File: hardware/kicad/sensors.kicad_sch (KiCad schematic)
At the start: 0 parts

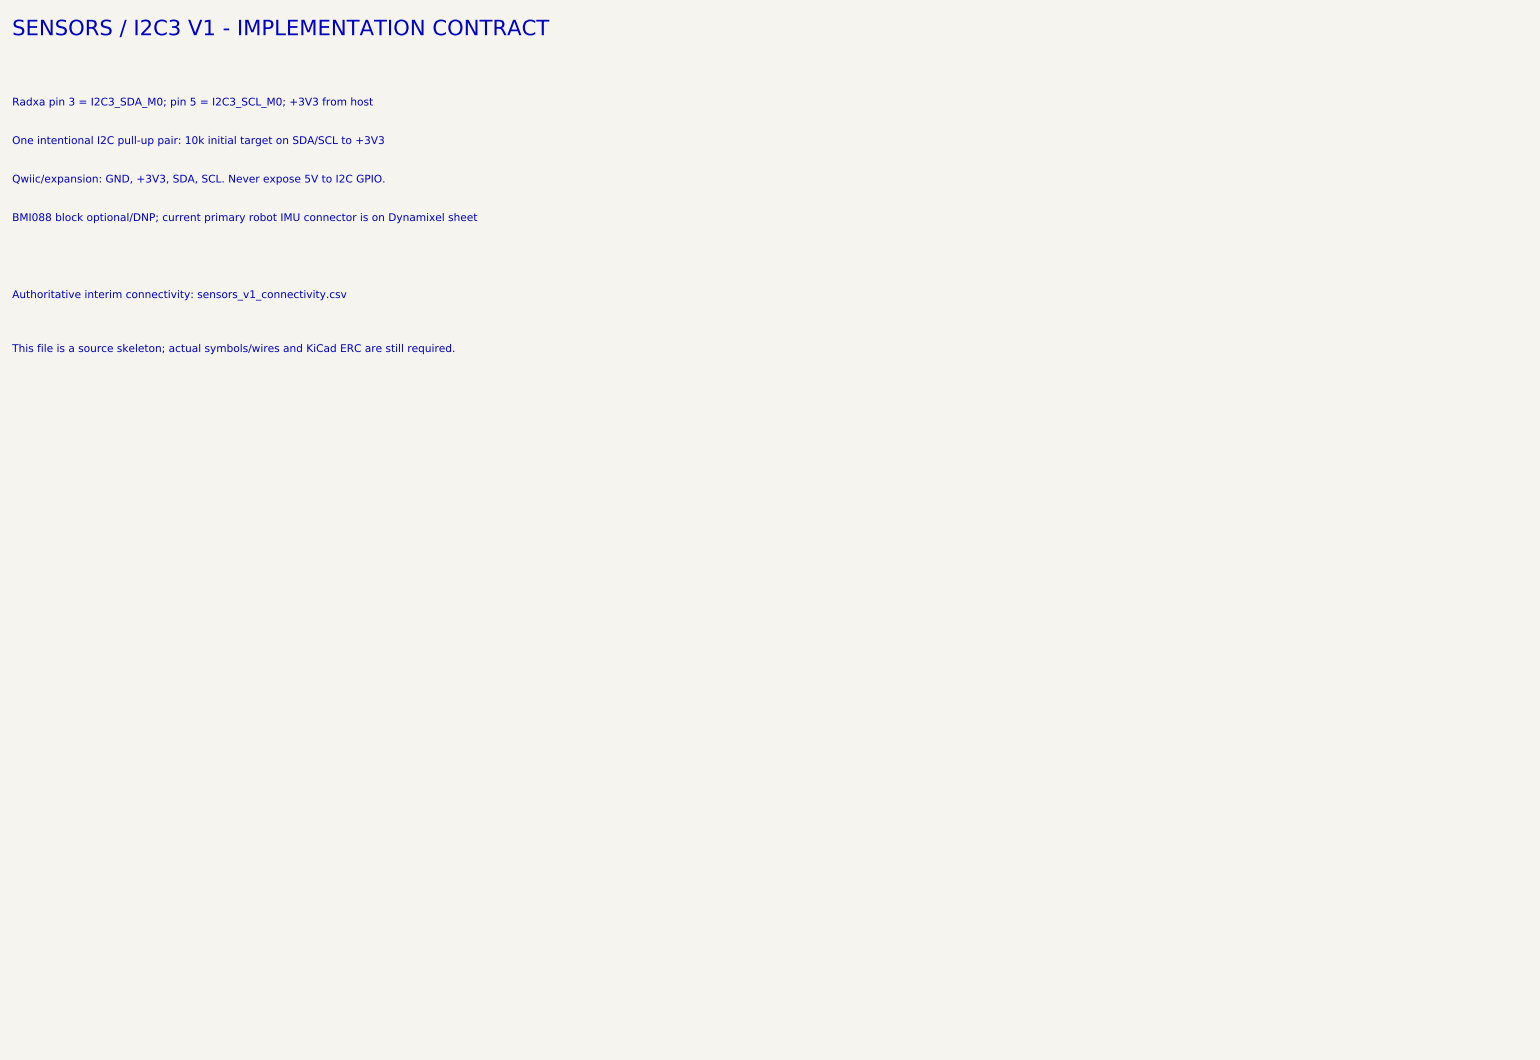
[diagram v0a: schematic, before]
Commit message: [verified] refactor(hardware): restore strict single-board Radxa port
Import the routed upstream Pollen Robot HAT as the active design, adapt the critical host nets for Radxa ZERO 3W, remove the divergent high-current redesign artifacts, and add regenerated baseline-aware KiCad validation.
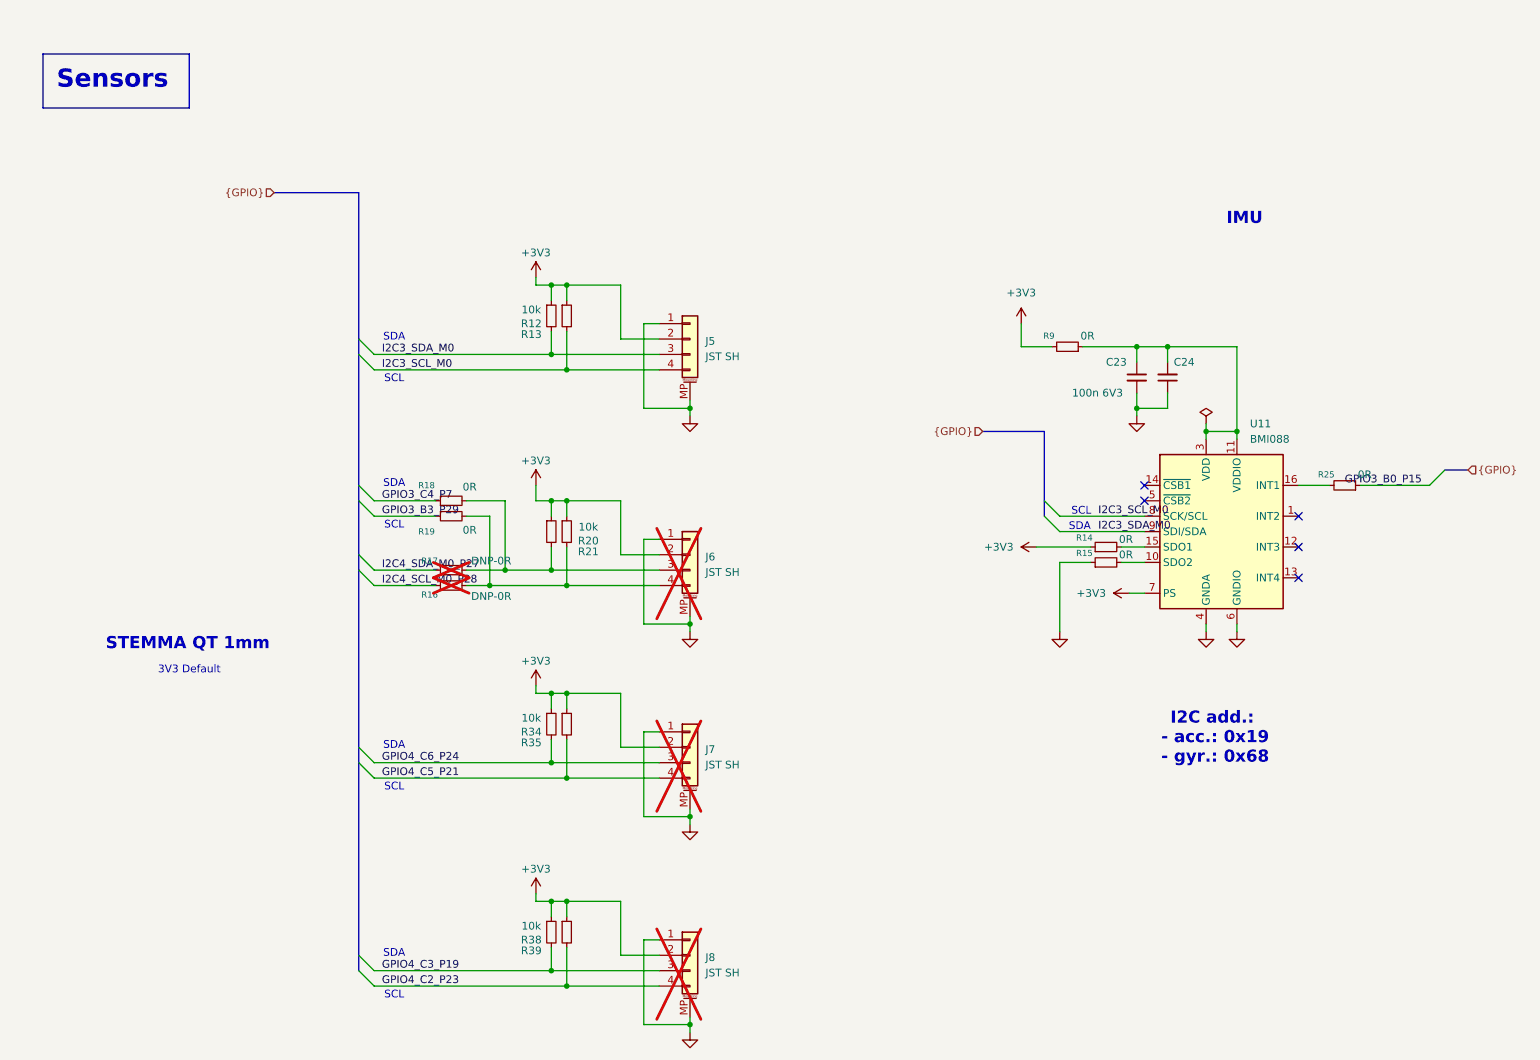
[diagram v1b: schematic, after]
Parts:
- added C23, C24: 100n 6V3, Capacitor_SMD:C_0402_1005Metric, symbol Device:C_Small
- added J5, J6, J7, J8: JST SH, Connector_JST:JST_SH_BM04B-SRSS-TB_1x04-1MP_P1.00mm_Vertical, symbol Connector_Generic_MountingPin:Conn_01x04_MountingPin
- added R12, R13, R20, R21, R34, R35, R38, R39: 10k, Resistor_SMD:R_0402_1005Metric, symbol Device:R_Small
- added R14, R15, R18, R19, R25, R9: 0R, Resistor_SMD:R_0402_1005Metric, symbol Device:R_Small
- added R16, R17: DNP-0R, Resistor_SMD:R_0402_1005Metric, symbol Device:R_Small
- added U11: BMI088, Package_LGA:Bosch_LGA-16_4.5x3mm_P0.5mm_LayoutBorder7x1y_ClockwisePinNumbering, symbol Sensor_Motion:BMI088
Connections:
- new net: J6.4 (Pin_4), R16.2, R19.2, R21.2
- new net: J6.3 (Pin_3), R17.2, R18.2, R20.2
- new net: R25.2, U11.16 (INT1)
- new net: R15.2, U11.10 (SDO2)
- new net: C23.1, C24.2, R9.1, U11.11 (VDDIO), U11.3 (VDD)
- new net: R14.2, U11.15 (SDO1)
- new net +3V3: J5.2 (Pin_2), J6.2 (Pin_2), J7.2 (Pin_2), J8.2 (Pin_2), R12.1, R13.1, R14.1, R20.1, R21.1, R34.1, R35.1, R38.1, R39.1, R9.2, U11.7 (PS)
- new net GND: C23.2, C24.1, J5.1 (Pin_1), J5.MP (MountPin), J6.1 (Pin_1), J6.MP (MountPin), J7.1 (Pin_1), J7.MP (MountPin), J8.1 (Pin_1), J8.MP (MountPin), R15.1, U11.2 (GNDA), U11.4 (GNDA), U11.6 (GNDIO)
- new net GPIO3_B0_P15: R25.1
- new net GPIO3_B3_P29: R19.1
- new net GPIO3_C4_P7: R18.1
- new net GPIO4_C2_P23: J8.4 (Pin_4), R39.2
- new net GPIO4_C3_P19: J8.3 (Pin_3), R38.2
- new net GPIO4_C5_P21: J7.4 (Pin_4), R35.2
- new net GPIO4_C6_P24: J7.3 (Pin_3), R34.2
- new net I2C3_SCL_M0: J5.4 (Pin_4), R13.2, U11.8 (SCK/SCL)
- new net I2C3_SDA_M0: J5.3 (Pin_3), R12.2, U11.9 (SDI/SDA)
- new net I2C4_SCL_M0_P28: R16.1
- new net I2C4_SDA_M0_P27: R17.1
- no-connect marks 0 -> 5
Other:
- note added: "3V3 Default"
- note added: "I2C add.: - acc.: 0x19 - gyr.: 0x68"
- note added: "IMU"
- note added: "SCL"
- note added: "SDA"
- note added: "STEMMA QT 1mm"
- note removed: "Authoritative interim connectivity: sensors_v1_connectivity.csv"
- note removed: "BMI088 block optional/DNP; current primary robot IMU connector is on Dynamixel sheet"
- note removed: "One intentional I2C pull-up pair: 10k initial target on SDA/SCL to +3V3"
- note removed: "Qwiic/expansion: GND, +3V3, SDA, SCL. Never expose 5V to I2C GPIO."
- note removed: "Radxa pin 3 = I2C3_SDA_M0; pin 5 = I2C3_SCL_M0; +3V3 from host"
- note removed: "SENSORS / I2C3 V1 - IMPLEMENTATION CONTRACT"
- note removed: "This file is a source skeleton; actual symbols/wires and KiCad ERC are still required."
- company: juper007 / DIY -> Pollen Robotics / Hugging Face
- title: Radxa ZERO 3W Robot HAT - Sensors / I2C V1 -> Radxa ZERO 3W Robot HAT

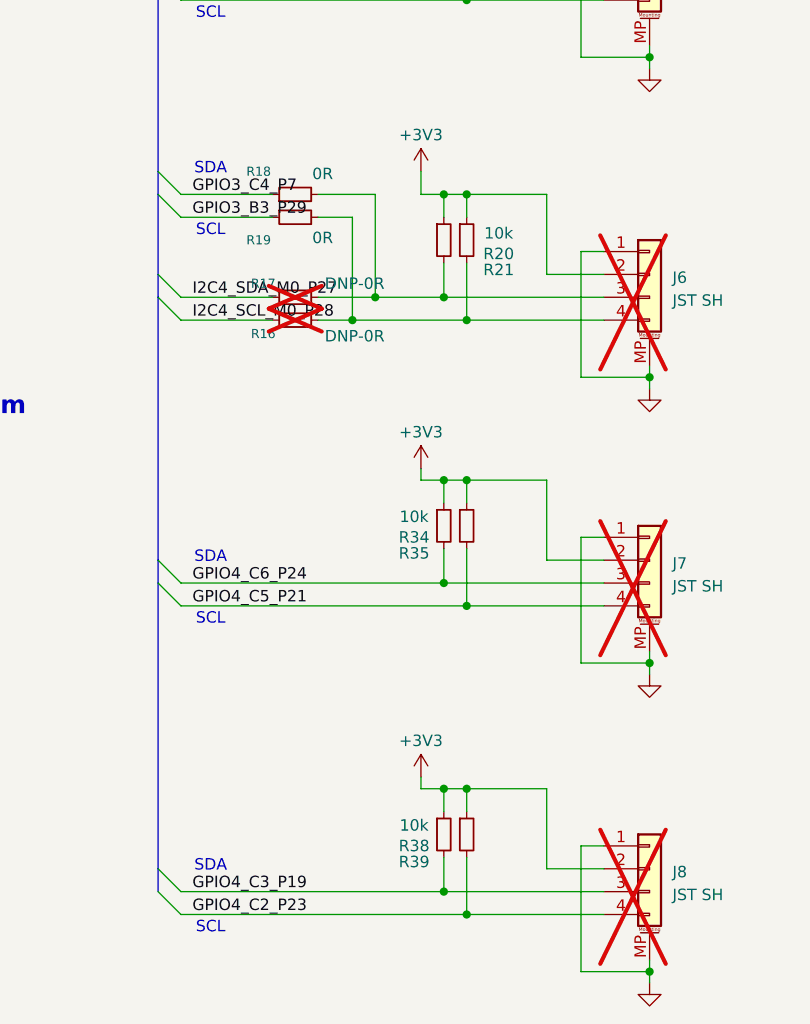
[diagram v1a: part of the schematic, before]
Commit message: [verified] fix(validation): enforce fail-closed strict-port guards
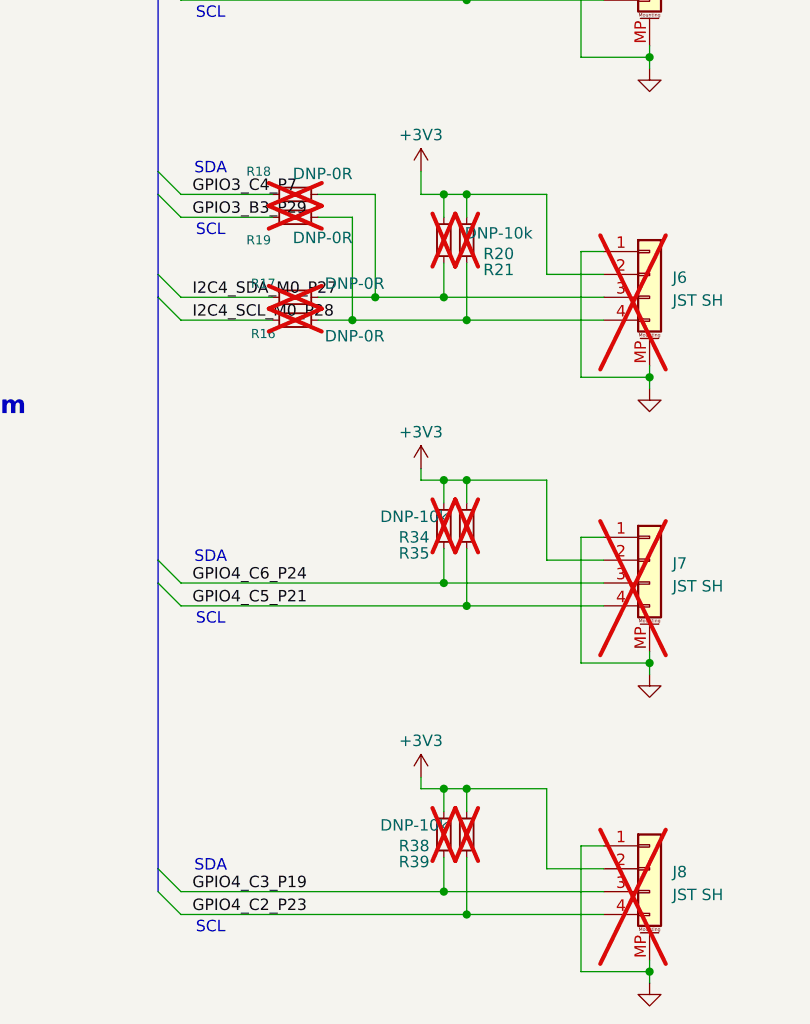
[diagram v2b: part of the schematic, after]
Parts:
- R18, R19: value 0R -> DNP-0R; now not fitted
- R20, R21, R34, R35, R38, R39: value 10k -> DNP-10k; now not fitted
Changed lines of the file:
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@@
 		(in_bom yes)
 		(on_board yes)
-		(dnp no)
+		(dnp yes)
 		(property "Reference" "R19"
 			(at 88.646 101.6 90)
@@
 			)
 		)
-		(property "Value" "0R"
+		(property "Value" "DNP-0R"
 			(at 95.758 101.346 90)
 			(effects
@@
 		(in_bom yes)
 		(on_board yes)
-		(dnp no)
+		(dnp yes)
 		(property "Reference" "R34"
 			(at 105.918 134.62 0)
@@
 			)
 		)
-		(property "Value" "10k"
+		(property "Value" "DNP-10k"
 			(at 105.918 132.334 0)
 			(effects
@@
 		(in_bom yes)
 		(on_board yes)
-		(dnp no)
+		(dnp yes)
 		(property "Reference" "R18"
 			(at 88.646 93.98 90)
@@
 			)
 		)
-		(property "Value" "0R"
+		(property "Value" "DNP-0R"
 			(at 95.758 94.234 90)
 			(effects
@@
 		(in_bom yes)
 		(on_board yes)
-		(dnp no)
+		(dnp yes)
 		(property "Reference" "R21"
 			(at 115.316 104.902 0)
@@
 			)
 		)
-		(property "Value" "10k"
+		(property "Value" "DNP-10k"
 			(at 108.458 103.124 0)
 			(effects
@@
 		(in_bom yes)
 		(on_board yes)
-		(dnp no)
+		(dnp yes)
 		(property "Reference" "R39"
 			(at 105.918 170.688 0)
@@
 			)
 		)
-		(property "Value" "10k"
+		(property "Value" "DNP-10k"
 			(at 108.458 169.164 0)
 			(effects
@@
 		(in_bom yes)
 		(on_board yes)
-		(dnp no)
+		(dnp yes)
 		(property "Reference" "R20"
 			(at 115.316 103.124 0)
@@
 			)
 		)
-		(property "Value" "10k"
+		(property "Value" "DNP-10k"
 			(at 115.316 100.838 0)
 			(effects
@@
 		(in_bom yes)
 		(on_board yes)
-		(dnp no)
+		(dnp yes)
 		(property "Reference" "R38"
 			(at 105.918 168.91 0)
@@
 			)
 		)
-		(property "Value" "10k"
+		(property "Value" "DNP-10k"
 			(at 105.918 166.624 0)
 			(effects
@@
 		(in_bom yes)
 		(on_board yes)
-		(dnp no)
+		(dnp yes)
 		(property "Reference" "R35"
 			(at 105.918 136.398 0)
@@
 			)
 		)
-		(property "Value" "10k"
+		(property "Value" "DNP-10k"
 			(at 108.458 134.874 0)
 			(effects

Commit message: [verified] feat(hardware): restore full Robot HAT connector parity
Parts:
- J6, J7, J8: now fitted
- R18, R19: value DNP-0R -> 0R; now fitted
- R20, R21, R34, R35, R38, R39: value DNP-10k -> 10k; now fitted
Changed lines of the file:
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@@
 		(in_bom yes)
 		(on_board yes)
-		(dnp yes)
+		(dnp no)
 		(property "Reference" "R19"
 			(at 88.646 101.6 90)
@@
 			)
 		)
-		(property "Value" "DNP-0R"
+		(property "Value" "0R"
 			(at 95.758 101.346 90)
 			(effects
@@
 		(in_bom yes)
 		(on_board yes)
-		(dnp yes)
+		(dnp no)
 		(property "Reference" "R34"
 			(at 105.918 134.62 0)
@@
 			)
 		)
-		(property "Value" "DNP-10k"
+		(property "Value" "10k"
 			(at 105.918 132.334 0)
 			(effects
@@
 		(in_bom yes)
 		(on_board yes)
-		(dnp yes)
+		(dnp no)
 		(property "Reference" "R18"
 			(at 88.646 93.98 90)
@@
 			)
 		)
-		(property "Value" "DNP-0R"
+		(property "Value" "0R"
 			(at 95.758 94.234 90)
 			(effects
@@
 		(in_bom yes)
 		(on_board yes)
-		(dnp yes)
+		(dnp no)
 		(fields_autoplaced yes)
 		(property "Reference" "J6"
@@
 		(in_bom yes)
 		(on_board yes)
-		(dnp yes)
+		(dnp no)
 		(property "Reference" "R21"
 			(at 115.316 104.902 0)
@@
 			)
 		)
-		(property "Value" "DNP-10k"
+		(property "Value" "10k"
 			(at 108.458 103.124 0)
 			(effects
@@
 		(in_bom yes)
 		(on_board yes)
-		(dnp yes)
+		(dnp no)
 		(property "Reference" "R39"
 			(at 105.918 170.688 0)
@@
 			)
 		)
-		(property "Value" "DNP-10k"
+		(property "Value" "10k"
 			(at 108.458 169.164 0)
 			(effects
@@
 		(in_bom yes)
 		(on_board yes)
-		(dnp yes)
+		(dnp no)
 		(property "Reference" "R20"
 			(at 115.316 103.124 0)
@@
 			)
 		)
-		(property "Value" "DNP-10k"
+		(property "Value" "10k"
 			(at 115.316 100.838 0)
 			(effects
@@
 		(in_bom yes)
 		(on_board yes)
-		(dnp yes)
+		(dnp no)
 		(property "Reference" "R38"
 			(at 105.918 168.91 0)
@@
 			)
 		)
-		(property "Value" "DNP-10k"
+		(property "Value" "10k"
 			(at 105.918 166.624 0)
 			(effects
@@
 		(in_bom yes)
 		(on_board yes)
-		(dnp yes)
+		(dnp no)
 		(property "Reference" "R35"
 			(at 105.918 136.398 0)
@@
 			)
 		)
-		(property "Value" "DNP-10k"
+		(property "Value" "10k"
 			(at 108.458 134.874 0)
 			(effects
@@
 		(in_bom yes)
 		(on_board yes)
-		(dnp yes)
+		(dnp no)
 		(fields_autoplaced yes)
 		(property "Reference" "J8"
@@
 		(in_bom yes)
 		(on_board yes)
-		(dnp yes)
+		(dnp no)
 		(fields_autoplaced yes)
 		(property "Reference" "J7"
